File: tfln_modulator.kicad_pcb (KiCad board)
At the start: 12 copper layers, 300 x 140 mm, 981 parts

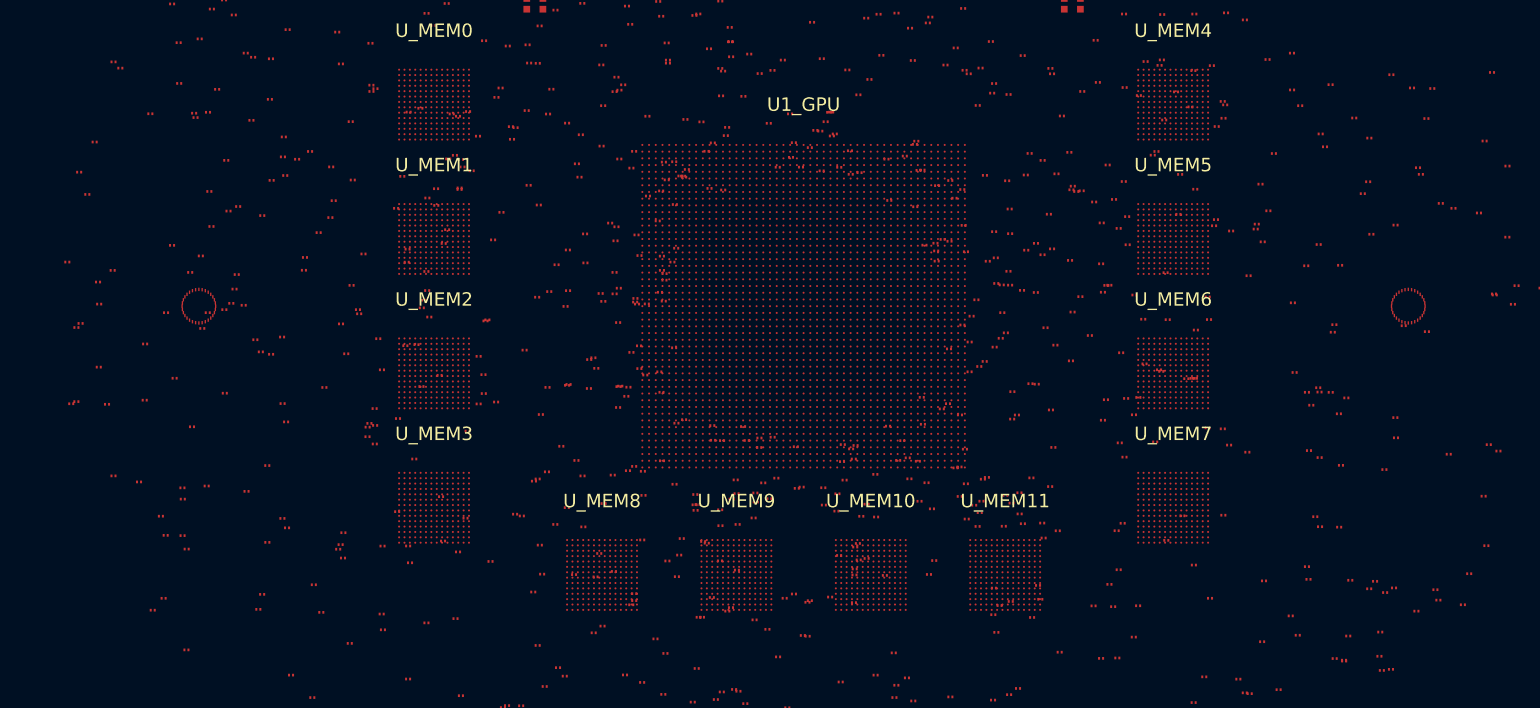
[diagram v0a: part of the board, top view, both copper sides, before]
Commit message: Generated 15-layer KiCad and Gerber files
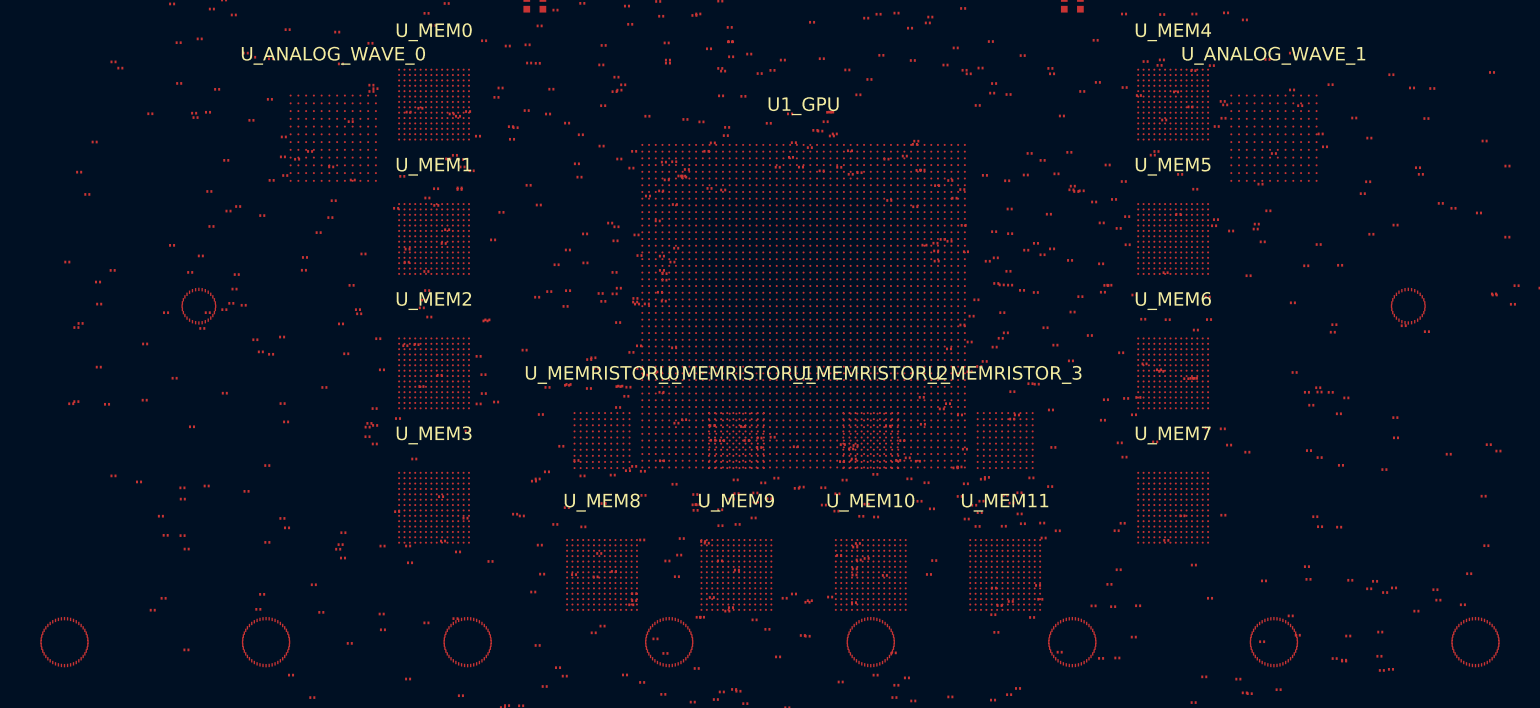
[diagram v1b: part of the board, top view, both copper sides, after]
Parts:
- added ?: , Package:QFN-48, F.Cu at (30.0, 120.0)
- added ?: , Package:QFN-48, F.Cu at (60.0, 120.0)
- added ?: , Package:QFN-48, F.Cu at (90.0, 120.0)
- added ?: , Package:QFN-48, F.Cu at (120.0, 120.0)
- added ?: , Package:QFN-48, F.Cu at (150.0, 120.0)
- added ?: , Package:QFN-48, F.Cu at (180.0, 120.0)
- added ?: , Package:QFN-48, F.Cu at (210.0, 120.0)
- added ?: , Package:QFN-48, F.Cu at (240.0, 120.0)
- added U_ANALOG_WAVE_0: , BGA:U_ANALOG_WAVE_0, F.Cu at (70.0, 45.0)
- added U_ANALOG_WAVE_1: , BGA:U_ANALOG_WAVE_1, F.Cu at (210.0, 45.0)
- added U_MEMRISTOR_0: , BGA:U_MEMRISTOR_0, F.Cu at (110.0, 90.0)
- added U_MEMRISTOR_1: , BGA:U_MEMRISTOR_1, F.Cu at (130.0, 90.0)
- added U_MEMRISTOR_2: , BGA:U_MEMRISTOR_2, F.Cu at (150.0, 90.0)
- added U_MEMRISTOR_3: , BGA:U_MEMRISTOR_3, F.Cu at (170.0, 90.0)
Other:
- copper layers 12 -> 15

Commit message: Increase component density to 2095 discrete components per user request
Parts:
- removed the ? at (177.6, 50.3)
- removed the ? at (178.6, 24.2)
- removed the ? at (206.0, 91.7)
- removed the ? at (235.9, 22.1)
- removed the ? at (154.4, 132.1)
- removed the ? at (192.3, 90.2)
- removed the ? at (193.9, 65.0)
- removed the ? at (149.3, 27.1)
- removed the ? at (86.0, 98.3)
- removed the ? at (246.1, 66.9)
- removed the ? at (130.2, 102.5)
- removed the ? at (45.8, 18.8)
- removed the ? at (118.3, 57.3)
- removed the ? at (179.3, 17.9)
- removed the ? at (173.1, 61.7)
- removed the ? at (150.7, 95.0)
- removed the ? at (170.0, 98.2)
- removed the ? at (86.2, 19.9)
- removed the ? at (90.1, 41.0)
- removed the ? at (201.5, 43.3)
- removed the ? at (131.9, 32.5)
- removed the ? at (107.1, 95.3)
- removed the ? at (140.6, 21.5)
- removed the ? at (114.4, 76.9)
- removed the ? at (249.8, 67.3)
- removed the ? at (146.1, 95.9)
- removed the ? at (180.1, 52.1)
- removed the ? at (169.2, 114.6)
- removed the ? at (214.8, 64.0)
- removed the ? at (218.8, 73.9)
- removed the ? at (213.9, 40.2)
- removed the ? at (164.0, 91.3)
- removed the ? at (112.0, 60.3)
- removed the ? at (104.8, 42.8)
- removed the ? at (193.0, 34.2)
- removed the ? at (220.4, 122.7)
- removed the ? at (130.3, 127.3)
- removed the ? at (142.7, 49.9)
- removed the ? at (57.8, 42.3)
- removed the ? at (198.4, 73.6)
- removed the ? at (159.9, 52.1)
- removed the ? at (42.8, 41.4)
- removed the ? at (57.4, 22.9)
- removed the ? at (163.2, 93.9)
- removed the ? at (178.4, 41.7)
- removed the ? at (173.9, 95.6)
- removed the ? at (207.3, 9.98)
- removed the ? at (98.9, 31.1)
- removed the ? at (170.7, 55.5)
- removed the ? at (236.7, 55.4)
- removed the ? at (208.3, 6.96)
- removed the ? at (138.1, 47.8)
- removed the ? at (185.3, 49.0)
- removed the ? at (210.7, 127.1)
- removed the ? at (156.3, 33.4)
- removed the ? at (119.1, 127.8)
- removed the ? at (147.7, 90.7)
- removed the ? at (172.6, 32.7)
- removed the ? at (77.2, 115.8)
- removed the ? at (34.5, 45.6)
- removed the ? at (112.7, 81.9)
- removed the ? at (65.6, 64.7)
- removed the ? at (91.5, 44.7)
- removed the ? at (129.0, 28.5)
- removed the ? at (158.0, 60.9)
- removed the ? at (187.8, 92.5)
- removed the ? at (167.9, 30.6)
- removed the ? at (99.9, 96.0)
- removed the ? at (124.1, 123.9)
- removed the ? at (112.4, 85.1)
- removed the ? at (95.0, 56.0)
- removed the ? at (135.4, 89.5)
- removed the ? at (88.6, 41.7)
- removed the ? at (63.0, 87.2)
- removed the ? at (153.5, 128.2)
- removed the ? at (190.9, 33.6)
- removed the ? at (112.5, 67.3)
- removed the ? at (177.5, 75.8)
- removed the ? at (98.5, 76.5)
- removed the ? at (226.6, 112.6)
- removed the ? at (100.7, 28.3)
- removed the ? at (127.6, 34.6)
- removed the ? at (142.4, 134.4)
- removed the ? at (219.0, 72.8)
- removed the ? at (113.6, 83.4)
- removed the ? at (174.6, 60.6)
- removed the ? at (203.3, 90.7)
- removed the ? at (164.6, 35.4)
- removed the ? at (159.4, 12.1)
- removed the ? at (219.8, 63.9)
- removed the ? at (210.0, 47.3)
- removed the ? at (55.3, 67.5)
- removed the ? at (49.5, 41.9)
- removed the ? at (136.4, 132.6)
- removed the ? at (112.6, 37.8)
- removed the ? at (51.9, 58.1)
- removed the ? at (134.0, 96.3)
- removed the ? at (121.1, 110.3)
- removed the ? at (184.3, 122.4)
- removed the ? at (125.9, 31.7)
- removed the ? at (216.9, 102.8)
- removed the ? at (85.3, 55.0)
- removed the ? at (155.4, 125.3)
- removed the ? at (187.8, 37.5)
- removed the ? at (194.2, 72.0)
- removed the ? at (141.1, 18.4)
- removed the ? at (232.7, 42.1)
- removed the ? at (139.1, 12.3)
- removed the ? at (84.9, 28.2)
- removed the ? at (147.6, 109.1)
- removed the ? at (216.6, 82.1)
- removed the ? at (198.2, 80.7)
- removed the ? at (118.4, 24.6)
- removed the ? at (168.7, 118.5)
- removed the ? at (183.2, 114.6)
- removed the ? at (214.9, 82.8)
- removed the ? at (89.0, 48.2)
- removed the ? at (126.0, 52.5)
- removed the ? at (108.7, 77.7)
- removed the ? at (122.2, 86.9)
- removed the ? at (121.9, 104.6)
- removed the ? at (147.5, 114.1)
- removed the ? at (75.8, 130.9)
- removed the ? at (177.2, 91.0)
- removed the ? at (118.9, 64.7)
- removed the ? at (152.6, 87.9)
- removed the ? at (124.8, 42.6)
- removed the ? at (112.6, 48.1)
- removed the ? at (205.7, 127.5)
- removed the ? at (231.4, 49.4)
- removed the ? at (169.3, 74.8)
- removed the ? at (118.8, 26.8)
- removed the ? at (225.7, 122.1)
- removed the ? at (55.4, 134.2)
- removed the ? at (214.9, 108.8)
- removed the ? at (82.7, 11.1)
- removed the ? at (144.1, 41.1)
- removed the ? at (62.1, 13.1)
- removed the ? at (170.7, 66.9)
- removed the ? at (99.8, 112.5)
- removed the ? at (104.5, 125.1)
- removed the ? at (168.6, 62.8)
- removed the ? at (63.1, 103.0)
- removed the ? at (197.0, 80.8)
- removed the ? at (224.0, 51.5)
- removed the ? at (155.8, 28.6)
- removed the ? at (71.9, 77.1)
- removed the ? at (133.0, 11.2)
- removed the ? at (166.3, 34.6)
- removed the ? at (221.1, 119.1)
- removed the ? at (92.4, 30.5)
- removed the ? at (193.2, 79.7)
- removed the ? at (151.6, 32.7)
- removed the ? at (177.0, 35.4)
- removed the ? at (100.3, 68.7)
- removed the ? at (159.8, 63.3)
- removed the ? at (134.8, 42.8)
- removed the ? at (143.3, 6.11)
- removed the ? at (157.1, 8.15)
- removed the ? at (145.0, 97.9)
- removed the ? at (68.7, 82.1)
- removed the ? at (79.5, 100.6)
- removed the ? at (171.0, 99.3)
- removed the ? at (167.3, 95.5)
- removed the ? at (147.7, 105.8)
- removed the ? at (147.1, 91.2)
- removed the ? at (129.9, 7.23)
- removed the ? at (33.4, 53.4)
- removed the ? at (176.7, 96.8)
- removed the ? at (145.3, 107.1)
- removed the ? at (176.0, 73.2)
- removed the ? at (38.3, 34.6)
- removed the ? at (198.1, 129.0)
- removed the ? at (42.0, 75.6)
- removed the ? at (51.9, 25.8)
- removed the ? at (82.1, 92.7)
- removed the ? at (64.6, 48.1)
- removed the ? at (174.7, 81.6)
- removed the ? at (36.3, 84.6)
- removed the ? at (63.7, 124.9)
- removed the ? at (121.7, 50.6)
- removed the ? at (154.7, 90.0)
- removed the ? at (70.3, 15.0)
- removed the ? at (76.2, 90.5)
- removed the ? at (178.2, 23.9)
- removed the ? at (81.4, 21.8)
- removed the ? at (222.0, 42.0)
- removed the ? at (106.3, 48.8)
- removed the ? at (149.4, 107.5)
- removed the ? at (171.8, 86.2)
- removed the ? at (120.7, 76.2)
- removed the ? at (129.1, 30.7)
- removed the ? at (60.2, 93.7)
- removed the ? at (212.7, 32.3)
- removed the ? at (75.7, 5.70)
- removed the ? at (212.7, 37.8)
- removed the ? at (84.0, 53.9)
- removed the ? at (205.7, 27.4)
- removed the ? at (232.8, 73.8)
- removed the ? at (225.1, 110.9)
- removed the ? at (127.6, 102.7)
- removed the ? at (60.7, 33.2)
- removed the ? at (172.6, 102.4)
- removed the ? at (35.2, 69.7)
- removed the ? at (196.4, 101.2)
- removed the ? at (118.5, 79.8)
- removed the ? at (139.9, 119.0)
- removed the ? at (167.4, 63.3)
- removed the ? at (55.2, 26.7)
- removed the ? at (168.3, 112.0)
- removed the ? at (245.6, 69.7)
- removed the ? at (140.9, 46.4)
- removed the ? at (103.8, 19.2)
- removed the ? at (91.9, 15.5)
- removed the ? at (194.0, 104.9)
- removed the ? at (114.3, 114.4)
- removed the ? at (190.3, 7.40)
- removed the ? at (122.8, 23.4)
- removed the ? at (183.2, 54.5)
- removed the ? at (51.4, 41.1)
- removed the ? at (163.3, 86.2)
- removed the ? at (116.0, 126.0)
- removed the ? at (188.2, 60.9)
- removed the ? at (83.9, 64.8)
- removed the ? at (81.1, 105.7)
- removed the ? at (116.2, 98.2)
- removed the ? at (77.9, 7.56)
- removed the ? at (202.4, 39.5)
- removed the ? at (121.0, 13.7)
- removed the ? at (170.5, 64.8)
- removed the ? at (107.5, 59.2)
- removed the ? at (63.5, 11.6)
- removed the ? at (198.1, 108.5)
- removed the ? at (233.3, 13.1)
- removed the ? at (185.5, 111.4)
- removed the ? at (45.1, 71.0)
- removed the ? at (55.6, 65.3)
- removed the ? at (162.6, 31.6)
- removed the ? at (88.2, 116.5)
- removed the ? at (37.2, 64.7)
- removed the ? at (151.2, 26.5)
- removed the ? at (192.5, 47.0)
- removed the ? at (207.3, 58.5)
- removed the ? at (168.2, 10.7)
- removed the ? at (126.3, 113.4)
- removed the ? at (212.8, 69.5)
- removed the ? at (178.1, 121.5)
- removed the ? at (101.5, 126.6)
- removed the ? at (72.9, 51.2)
- removed the ? at (113.4, 124.9)
- removed the ? at (128.0, 35.0)
- removed the ? at (226.4, 94.3)
- removed the ? at (69.8, 131.0)
- removed the ? at (88.8, 52.6)
- removed the ? at (31.8, 73.2)
- removed the ? at (116.7, 69.7)
- removed the ? at (190.0, 16.6)
- removed the ? at (48.2, 106.1)
- removed the ? at (75.1, 88.0)
- removed the ? at (68.2, 115.6)
- removed the ? at (201.1, 58.0)
- removed the ? at (122.2, 22.8)
- removed the ? at (186.8, 7.02)
- removed the ? at (118.0, 119.5)
- removed the ? at (70.4, 5.86)
- removed the ? at (236.0, 92.0)
- removed the ? at (122.2, 50.8)
- removed the ? at (242.9, 68.3)
- removed the ? at (60.2, 105.2)
- removed the ? at (120.7, 48.5)
- removed the ? at (47.6, 104.1)
- removed the ? at (207.7, 23.0)
- removed the ? at (146.9, 46.9)
- removed the ? at (107.2, 102.8)
- removed the ? at (107.5, 63.6)
- removed the ? at (53.7, 24.4)
- removed the ? at (171.0, 86.8)
- removed the ? at (175.6, 48.3)
- removed the ? at (108.1, 77.9)
- removed the ? at (138.6, 112.8)
- removed the ? at (147.0, 50.4)
- removed the ? at (108.0, 82.2)
- removed the ? at (96.4, 43.3)
- removed the ? at (71.1, 105.5)
- removed the ? at (164.0, 34.9)
- removed the ? at (111.6, 95.1)
- removed the ? at (220.0, 93.7)
- removed the ? at (145.1, 133.3)
- removed the ? at (76.3, 37.6)
- removed the ? at (99.1, 52.0)
- removed the ? at (120.8, 54.9)
- removed the ? at (193.3, 33.3)
- removed the ? at (153.8, 26.4)
- removed the ? at (95.3, 129.7)
- removed the ? at (84.0, 16.8)
- removed the ? at (202.9, 26.3)
- removed the ? at (87.6, 41.4)
- removed the ? at (130.1, 109.3)
- removed the ? at (212.5, 116.1)
- removed the ? at (139.3, 23.4)
- removed the ? at (164.2, 96.4)
- removed the ? at (207.4, 57.8)
- removed the ? at (198.0, 34.9)
- removed the ? at (46.4, 80.7)
- removed the ? at (177.8, 103.4)
- removed the ? at (224.5, 59.3)
- removed the ? at (153.4, 18.8)
- removed the ? at (119.3, 65.2)
- removed the ? at (142.9, 97.0)
- removed the ? at (111.6, 16.1)
- removed the ? at (70.6, 29.2)
- removed the ? at (227.5, 35.5)
- removed the ? at (143.0, 99.6)
- removed the ? at (156.6, 55.2)
- removed the ? at (200.8, 34.2)
- removed the ? at (176.8, 85.4)
- removed the ? at (219.3, 19.2)
- removed the ? at (100.4, 95.7)
- removed the ? at (170.7, 59.2)
- removed the ? at (134.9, 98.6)
- removed the ? at (92.7, 72.2)
- removed the ? at (161.8, 51.3)
- removed the ? at (109.1, 79.2)
- removed the ? at (48.1, 121.2)
- removed the ? at (186.6, 103.4)
- removed the ? at (86.3, 105.0)
- removed the ? at (243.4, 91.6)
- removed the ? at (90.0, 88.6)
- removed the ? at (128.6, 43.4)
- removed the ? at (208.3, 60.4)
- removed the ? at (89.0, 128.0)
- removed the ? at (98.1, 101.2)
- removed the ? at (166.7, 95.7)
- removed the ? at (47.5, 97.0)
- removed the ? at (89.9, 8.09)
- removed the ? at (213.1, 79.9)
- removed the ? at (111.2, 57.6)
- removed the ? at (142.5, 43.9)
- removed the ? at (148.2, 107.8)
- removed the ? at (167.0, 50.5)
- removed the ? at (152.8, 54.3)
- removed the ? at (153.4, 121.6)
- removed the ? at (162.6, 94.1)
- removed the ? at (159.4, 107.9)
- removed the ? at (218.5, 82.8)
- removed the ? at (145.3, 49.3)
- removed the ? at (121.5, 107.0)
- removed the ? at (173.8, 81.5)
- removed the ? at (54.4, 55.8)
- removed the ? at (53.9, 83.0)
- removed the ? at (50.3, 62.5)
- removed the ? at (110.2, 69.3)
- removed the ? at (180.6, 52.9)
- removed the ? at (241.2, 98.3)
- removed the ? at (75.4, 87.4)
- removed the ? at (239.1, 109.8)
- removed the ? at (88.6, 106.6)
- removed the ? at (58.4, 75.0)
- removed the ? at (231.2, 115.4)
- removed the ? at (118.8, 52.8)
- removed the ? at (135.9, 95.6)
- removed the ? at (66.5, 47.0)
- removed the ? at (189.2, 68.3)
- removed the ? at (79.4, 20.4)
- removed the ? at (75.1, 89.4)
- removed the ? at (200.5, 113.5)
- removed the ? at (148.2, 130.1)
- removed the ? at (91.6, 84.5)
- removed the ? at (187.5, 102.3)
- removed the ? at (110.3, 19.7)
- removed the ? at (170.8, 114.0)
- removed the ? at (234.0, 112.2)
- removed the ? at (219.0, 122.4)
- removed the ? at (138.0, 41.4)
- removed the ? at (135.4, 34.9)
- removed the ? at (52.7, 37.7)
- removed the ? at (72.6, 42.5)
- removed the ? at (175.7, 104.5)
- removed the ? at (113.7, 25.3)
- removed the ? at (199.1, 5.48)
- removed the ? at (223.2, 53.3)
- removed the ? at (95.9, 129.4)
- removed the ? at (156.8, 45.4)
- removed the ? at (144.2, 17.1)
- removed the ? at (234.8, 54.7)
- removed the ? at (114.8, 93.8)
- removed the ? at (69.2, 8.70)
- removed the ? at (216.8, 82.8)
- removed the ? at (158.7, 109.9)
- removed the ? at (190.5, 71.9)
- removed the ? at (50.1, 30.2)
- removed the ? at (175.2, 113.6)
- removed the ? at (215.6, 84.7)
- removed the ? at (108.8, 118.6)
- removed the ? at (130.5, 17.5)
- removed the ? at (58.1, 33.0)
- removed the ? at (112.0, 5.71)
- removed the ? at (166.1, 79.0)
- removed the ? at (114.8, 47.0)
- removed the ? at (60.7, 77.2)
- removed the ? at (131.3, 129.2)
- removed the ? at (206.4, 127.7)
- removed the ? at (127.8, 127.4)
- removed the ? at (59.2, 76.8)
- removed the ? at (216.8, 92.5)
- removed the ? at (94.9, 37.5)
- removed the ? at (133.4, 89.6)
- removed the ? at (179.8, 78.1)
- removed the ? at (165.4, 99.6)
- removed the ? at (119.7, 107.9)
- removed the ? at (139.6, 49.3)
- removed the ? at (113.9, 94.5)
- removed the ? at (56.7, 69.9)
- removed the ? at (157.1, 49.8)
- removed the ? at (163.6, 72.8)
- removed the ? at (75.7, 38.0)
- removed the ? at (67.1, 111.5)
- removed the ? at (170.1, 74.0)
- removed the ? at (134.6, 118.1)
- removed the ? at (155.6, 23.3)
- removed the ? at (227.4, 124.0)
- removed the ? at (67.8, 59.1)
- removed the ? at (119.4, 121.7)
- removed the ? at (114.8, 113.8)
- removed the ? at (104.9, 67.7)
- removed the ? at (109.8, 68.1)
- removed the ? at (150.8, 101.4)
- removed the ? at (50.5, 73.3)
- removed the ? at (193.7, 42.3)
- removed the ? at (176.5, 56.3)
- removed the ? at (93.3, 16.8)
- removed the ? at (190.1, 12.6)
- removed the ? at (184.6, 132.1)
- removed the ? at (115.6, 79.3)
- removed the ? at (132.7, 116.7)
- removed the ? at (115.0, 68.8)
- removed the ? at (94.2, 84.3)
- removed the ? at (152.3, 48.1)
- removed the ? at (157.7, 49.7)
- removed the ? at (67.3, 5.87)
- removed the ? at (77.4, 118.2)
- removed the ? at (76.2, 85.2)
- removed the ? at (44.3, 101.3)
- removed the ? at (91.6, 77.5)
- removed the ? at (171.1, 82.7)
- removed the ? at (163.6, 52.6)
- removed the ? at (128.7, 20.4)
- removed the ? at (170.6, 127.8)
- removed the ? at (100.9, 86.1)
- removed the ? at (81.1, 61.5)
- removed the ? at (116.1, 94.6)
- removed the ? at (41.1, 96.2)
- removed the ? at (101.8, 94.7)
- removed the ? at (98.8, 40.9)
- removed the ? at (161.5, 84.5)
- removed the ? at (96.6, 45.2)
- removed the ? at (120.8, 96.5)
- removed the ? at (94.3, 38.9)
- removed the ? at (153.9, 17.9)
- removed the ? at (59.4, 56.5)
- removed the ? at (70.7, 106.2)
- removed the ? at (105.8, 109.9)
- removed the ? at (140.9, 113.8)
- removed the ? at (148.1, 105.3)
- removed the ? at (35.1, 79.1)
- removed the ? at (166.2, 100.7)
- removed the ? at (155.1, 47.7)
- removed the ? at (143.8, 41.1)
- removed the ? at (210.9, 6.48)
- removed the ? at (127.9, 90.0)
- removed the ? at (168.2, 115.9)
- removed the ? at (89.7, 101.6)
- removed the ? at (126.9, 128.5)
- removed the ? at (198.2, 26.5)
- removed the ? at (57.1, 97.6)
- removed the ? at (115.2, 133.4)
- removed the ? at (49.0, 87.9)
- removed the ? at (244.7, 59.7)
- removed the ? at (127.8, 130.3)
- removed the ? at (86.4, 60.7)
- removed the ? at (113.2, 37.1)
- removed the ? at (47.1, 36.8)
- removed the ? at (156.6, 45.9)
- removed the ? at (196.0, 50.4)
- removed the ? at (150.7, 124.9)
- removed the ? at (101.9, 82.1)
- removed the ? at (190.7, 78.6)
- removed the ? at (115.2, 69.7)
- removed the ? at (181.2, 68.6)
- removed the ? at (192.9, 79.5)
- removed the ? at (132.6, 101.5)
- removed the ? at (131.0, 38.8)
- removed the ? at (200.3, 72.0)
- removed the ? at (139.0, 97.1)
- removed the ? at (49.3, 41.3)
- removed the ? at (30.4, 63.4)
- removed the ? at (55.8, 55.2)
- removed the ? at (132.9, 99.2)
- removed the ? at (185.0, 83.9)
- removed the ? at (155.7, 14.4)
- removed the ? at (186.9, 109.2)
- removed the ? at (56.7, 12.1)
- removed the ? at (118.6, 67.9)
- removed the ? at (165.9, 102.8)
- removed the ? at (96.0, 31.3)
- removed the ? at (103.9, 90.8)
- removed the ? at (167.0, 78.2)
- removed the ? at (208.5, 110.9)
- removed the ? at (238.1, 114.4)
- removed the ? at (72.7, 66.9)
- removed the ? at (37.3, 33.6)
- removed the ? at (85.8, 80.3)
- removed the ? at (216.7, 60.8)
- removed the ? at (182.6, 74.4)
- removed the ? at (80.5, 7.98)
- removed the ? at (188.0, 83.7)
- removed the ? at (166.9, 6.29)
- removed the ? at (119.2, 48.6)
- removed the ? at (146.5, 34.8)
- removed the ? at (119.2, 11.8)
- removed the ? at (144.2, 44.7)
- removed the ? at (123.5, 128.9)
- removed the ? at (147.5, 92.7)
- removed the ? at (161.7, 60.3)
- removed the ? at (206.2, 65.5)
- removed the ? at (150.0, 18.8)
- removed the ? at (118.9, 93.0)
- removed the ? at (32.4, 72.6)
- removed the ? at (59.4, 112.9)
- removed the ? at (197.6, 40.3)
- removed the ? at (161.1, 6.68)
- removed the ? at (215.1, 110.7)
- removed the ? at (110.1, 132.3)
- removed the ? at (125.6, 46.9)
- removed the ? at (102.0, 41.4)
- removed the ? at (118.4, 15.8)
- removed the ? at (189.8, 83.6)
- removed the ? at (242.5, 35.2)
- removed the ? at (122.6, 49.7)
- removed the ? at (121.1, 87.4)
- removed the ? at (156.6, 20.0)
- removed the ? at (217.6, 46.3)
- removed the ? at (114.4, 49.4)
- removed the ? at (228.2, 89.6)
- removed the ? at (144.6, 44.4)
- removed the ? at (100.7, 105.6)
- removed the ? at (83.9, 26.4)
- removed the ? at (217.0, 44.4)
- removed the ? at (144.4, 16.7)
- removed the ? at (69.6, 56.8)
- removed the ? at (32.2, 50.1)
- removed the ? at (107.1, 24.9)
- removed the ? at (172.1, 97.8)
- removed the ? at (53.8, 70.5)
- removed the ? at (89.2, 49.3)
- removed the ? at (137.2, 113.5)
- removed the ? at (200.1, 68.6)
- removed the ? at (179.6, 47.1)
- removed the ? at (186.1, 114.7)
- removed the ? at (47.6, 98.7)
- removed the ? at (45.1, 104.1)
- removed the ? at (136.2, 49.3)
- removed the ? at (128.4, 44.6)
- removed the ? at (187.1, 90.3)
- removed the ? at (193.4, 26.6)
- removed the ? at (48.7, 65.0)
- removed the ? at (149.4, 99.5)
- removed the ? at (148.2, 38.5)
- removed the ? at (118.9, 62.6)
- removed the ? at (157.6, 19.8)
- removed the ? at (86.9, 25.0)
- removed the ? at (129.9, 95.9)
- removed the ? at (60.8, 51.3)
- removed the ? at (224.2, 112.1)
- removed the ? at (114.3, 15.2)
- removed the ? at (176.7, 34.6)
- removed the ? at (175.6, 62.3)
- removed the ? at (189.9, 38.6)
- removed the ? at (157.8, 87.6)
- removed the ? at (157.3, 99.0)
- removed the ? at (127.6, 22.6)
- removed the ? at (187.7, 51.4)
- removed the ? at (111.9, 38.1)
- removed the ? at (112.2, 35.9)
- removed the ? at (189.1, 119.2)
- removed the ? at (93.8, 60.1)
- removed the ? at (171.9, 126.9)
- removed the ? at (180.9, 7.77)
- removed the ? at (172.2, 7.03)
- removed the ? at (161.6, 76.4)
- removed the ? at (71.1, 33.9)
- removed the ? at (103.1, 25.9)
- removed the ? at (94.8, 23.5)
- removed the ? at (184.4, 57.6)
- removed the ? at (112.4, 82.0)
- removed the ? at (161.4, 10.2)
- removed the ? at (164.7, 79.8)
- removed the ? at (80.7, 75.9)
- removed the ? at (109.9, 46.2)
- removed the ? at (130.5, 22.8)
- removed the ? at (90.6, 49.8)
- removed the ? at (92.4, 80.2)
- removed the ? at (140.6, 114.1)
- removed the ? at (132.8, 97.8)
- removed the ? at (99.2, 33.8)
- removed the ? at (198.3, 52.6)
- removed the ? at (168.1, 38.3)
- removed the ? at (123.9, 100.4)
- removed the ? at (51.3, 71.0)
- removed the ? at (73.7, 70.5)
- removed the ? at (187.3, 76.9)
- removed the ? at (35.0, 66.4)
- removed the ? at (189.2, 86.2)
- removed the ? at (187.7, 26.5)
- removed the ? at (62.5, 84.5)
- removed the ? at (179.2, 14.0)
- removed the ? at (168.2, 128.6)
- removed the ? at (183.5, 30.4)
- removed the ? at (97.1, 101.0)
- removed the ? at (202.5, 101.1)
- removed the ? at (185.1, 66.9)
- removed the ? at (199.6, 125.2)
- removed the ? at (102.1, 67.8)
- removed the ? at (202.4, 88.3)
- removed the ? at (123.9, 98.0)
- removed the ? at (79.6, 86.7)
- removed the ? at (65.8, 62.7)
- removed the ? at (109.9, 34.1)
- removed the ? at (102.5, 37.7)
- removed the ? at (174.6, 68.0)
- removed the ? at (163.7, 25.7)
- removed the ? at (158.9, 27.0)
- removed the ? at (115.5, 22.8)
- removed the ? at (46.4, 15.7)
- removed the ? at (220.8, 83.7)
- removed the ? at (201.4, 57.1)
- removed the ? at (174.7, 133.7)
- removed the ? at (84.1, 17.6)
- removed the ? at (182.9, 131.3)
- removed the ? at (219.7, 86.0)
- removed the ? at (131.5, 90.0)
- removed the ? at (127.7, 38.7)
- removed the ? at (148.9, 13.8)
- removed the ? at (219.7, 102.9)
- removed the ? at (148.6, 101.3)
- removed the ? at (114.2, 28.0)
- removed the ? at (113.8, 132.0)
- removed the ? at (170.3, 51.3)
- removed the ? at (109.0, 110.3)
- removed the ? at (54.1, 48.3)
- removed the ? at (100.6, 54.9)
- removed the ? at (179.7, 63.2)
- removed the ? at (128.6, 115.4)
- removed the ? at (129.2, 32.9)
- removed the ? at (111.8, 109.5)
- removed the ? at (172.2, 100.9)
- removed the ? at (81.1, 125.5)
- removed the ? at (129.2, 114.9)
- removed the ? at (137.6, 129.8)
- removed the ? at (158.7, 130.3)
- removed the ? at (51.6, 52.9)
- removed the ? at (202.5, 42.0)
- removed the ? at (193.8, 132.8)
- removed the ? at (75.5, 30.9)
- removed the ? at (119.8, 33.4)
- removed the ? at (96.1, 18.3)
- removed the ? at (118.9, 82.8)
- removed the ? at (208.2, 119.9)
- removed the ? at (229.3, 72.9)
- removed the ? at (202.7, 40.0)
- removed the ? at (192.0, 47.5)
- removed the ? at (131.0, 87.9)
- removed the ? at (41.9, 84.0)
- removed the ? at (177.0, 61.5)
- removed the ? at (110.2, 31.2)
- removed the ? at (226.1, 124.2)
- removed the ? at (70.1, 54.3)
- removed the ? at (218.4, 37.0)
- removed the ? at (242.8, 68.2)
- removed the ? at (84.3, 71.6)
- removed the ? at (241.4, 45.4)
- removed the ? at (121.0, 61.4)
- removed the ? at (159.6, 60.6)
- removed the ? at (169.5, 66.8)
- removed the ? at (185.5, 66.9)
- removed the ? at (71.2, 72.6)
- removed the ? at (161.8, 128.2)
- removed the ? at (155.7, 95.7)
- removed the ? at (137.2, 131.2)
- removed the ? at (136.9, 33.4)
- removed the ? at (57.0, 32.3)
- removed the ? at (217.4, 11.5)
- removed the ? at (46.0, 60.9)
- removed the ? at (184.6, 87.0)
- removed the ? at (126.5, 45.7)
- removed the ? at (163.2, 98.3)
- removed the ? at (140.6, 119.1)
- removed the ? at (143.9, 113.3)
- removed the ? at (224.2, 45.0)
- removed the ? at (132.0, 23.5)
- removed the ? at (128.0, 52.7)
- removed the ? at (216.2, 101.3)
- removed the ? at (129.3, 98.7)
- removed the ? at (83.5, 69.1)
- removed the ? at (233.6, 37.6)
- removed the ? at (175.5, 102.3)
- removed the ? at (158.3, 96.3)
- removed the ? at (71.3, 16.2)
- removed the ? at (85.3, 52.5)
- removed the ? at (79.4, 55.4)
- removed the ? at (141.3, 27.7)
- removed the ? at (225.8, 118.5)
- removed the ? at (122.8, 12.3)
- removed the ? at (115.1, 59.4)
- removed the ? at (115.6, 62.5)
- removed the ? at (112.4, 72.4)
- removed the ? at (81.2, 41.1)
- removed the ? at (124.2, 99.5)
- removed the ? at (189.8, 114.6)
- removed the ? at (106.6, 50.8)
- removed the ? at (111.9, 68.2)
- removed the ? at (51.2, 96.8)
- removed the ? at (76.2, 87.7)
- removed the ? at (115.5, 75.9)
- removed the ? at (162.6, 19.1)
- removed the ? at (63.2, 28.8)
- removed the ? at (141.7, 43.8)
- removed the ? at (126.5, 90.0)
- removed the ? at (165.7, 69.0)
- removed the ? at (234.5, 113.7)
- removed the ? at (242.0, 90.6)
- removed the ? at (146.8, 13.6)
- removed the ? at (228.1, 57.9)
- removed the ? at (71.4, 107.5)
- removed the ? at (221.9, 15.7)
- removed the ? at (117.9, 20.9)
- removed the ? at (62.9, 50.6)
- removed the ? at (201.5, 134.2)
- removed the ? at (94.6, 134.4)
- removed the ? at (104.9, 61.6)
- removed the ? at (180.0, 70.9)
- removed the ? at (133.4, 91.0)
- removed the ? at (62.5, 47.8)
- removed the ? at (170.2, 9.21)
- removed the ? at (116.0, 104.8)
- removed the ? at (181.4, 52.8)
- removed the ? at (204.7, 125.5)
- removed the ? at (58.8, 115.1)
- removed the ? at (80.3, 50.7)
- removed the ? at (206.3, 10.7)
- removed the ? at (145.8, 90.6)
- removed the ? at (168.4, 76.1)
- removed the ? at (138.6, 45.7)
- removed the ? at (145.5, 125.9)
- removed the ? at (165.9, 40.1)
- removed the ? at (114.9, 69.4)
- removed the ? at (158.5, 27.8)
- removed the ? at (124.4, 116.3)
- removed the ? at (122.4, 42.2)
- removed the ? at (170.5, 38.5)
- removed the ? at (127.6, 107.9)
- removed the ? at (164.2, 61.9)
- removed the ? at (224.3, 17.7)
- removed the ? at (71.5, 103.7)
- removed the ? at (203.6, 58.8)
- removed the ? at (174.0, 116.3)
- removed the ? at (141.5, 16.1)
- removed the ? at (176.6, 19.2)
- removed the ? at (127.6, 24.6)
- removed the ? at (219.6, 22.8)
- removed the ? at (153.8, 126.4)
- removed the ? at (209.2, 55.8)
- removed the ? at (186.7, 122.4)
- removed the ? at (152.1, 110.1)
- removed the ? at (209.1, 33.3)
- removed the ? at (220.5, 122.8)
- removed the ? at (119.6, 30.8)
- removed the ? at (192.1, 17.0)
- removed the ? at (142.7, 33.2)
- removed the ? at (60.6, 39.2)
- removed the ? at (183.1, 23.8)
- removed the ? at (125.6, 105.3)
- removed the ? at (188.2, 56.7)
- removed the ? at (159.7, 61.8)
- removed the ? at (31.0, 84.5)
- removed the ? at (106.8, 44.5)
- removed the ? at (173.1, 50.5)
- removed the ? at (86.9, 58.6)
- removed the ? at (136.2, 122.2)
- removed the ? at (73.9, 71.1)
- removed the ? at (168.7, 66.6)
- removed the ? at (173.3, 17.4)
- removed the ? at (80.9, 63.5)
- removed the ? at (87.1, 48.1)
- removed the ? at (164.3, 101.7)
- removed the ? at (179.9, 52.7)
- removed the ? at (77.3, 105.7)
- removed the ? at (123.8, 99.6)
- removed the ? at (167.1, 23.1)
- removed the ? at (103.4, 16.4)
- removed the ? at (231.9, 50.4)
- removed the ? at (62.4, 74.6)
- removed the ? at (149.8, 36.3)
- removed the ? at (144.9, 100.5)
- removed the ? at (133.5, 35.4)
- removed the ? at (195.4, 38.1)
- removed the ? at (96.8, 16.5)
- removed the ? at (164.7, 75.3)
- removed the ? at (230.6, 37.5)
- removed the ? at (171.4, 22.3)
- removed the ? at (129.1, 30.6)
- removed the ? at (119.2, 69.2)
- removed the ? at (100.4, 33.9)
- removed the ? at (80.5, 16.5)
- removed the ? at (97.1, 43.4)
- removed the ? at (76.7, 74.8)
- removed the ? at (120.5, 63.4)
- removed the ? at (119.3, 66.1)
- removed the ? at (184.3, 63.7)
- removed the ? at (148.3, 50.1)
- removed the ? at (219.7, 133.5)
- removed the ? at (157.0, 93.1)
- removed the ? at (103.2, 63.8)
- removed the ? at (101.1, 109.9)
- removed the ? at (88.1, 47.5)
- removed the ? at (147.6, 110.0)
- removed the ? at (189.6, 8.70)
- removed the ? at (213.5, 119.0)
- removed the ? at (88.8, 52.4)
- removed the ? at (165.0, 71.5)
- removed the ? at (104.6, 70.0)
- removed the ? at (152.7, 12.3)
- removed the ? at (184.5, 14.8)
- removed the ? at (111.9, 65.0)
- removed the ? at (145.7, 93.1)
- removed the ? at (214.6, 6.29)
- removed the ? at (122.1, 50.6)
- removed the ? at (200.1, 88.1)
- removed the ? at (163.8, 58.0)
- removed the ? at (47.0, 30.8)
- removed the ? at (160.7, 60.1)
- removed the ? at (186.9, 58.4)
- removed the ? at (72.5, 120.2)
- removed the ? at (154.1, 93.0)
- removed the ? at (161.1, 34.1)
- removed the ? at (183.8, 36.7)
- removed the ? at (141.8, 20.2)
- removed the ? at (173.6, 47.3)
- removed the ? at (172.5, 67.6)
- removed the ? at (54.8, 69.6)
- removed the ? at (241.6, 105.6)
- removed the ? at (171.4, 19.6)
- removed the ? at (146.0, 19.7)
- removed the ? at (55.6, 134.0)
- removed the ? at (228.1, 86.6)
- removed the ? at (184.6, 67.9)
- removed the ? at (100.4, 120.5)
- removed the ? at (44.8, 113.5)
- removed the ? at (227.9, 111.9)
- removed the ? at (119.6, 51.2)
- removed the ? at (155.5, 92.6)
- removed the ? at (84.0, 7.34)
- removed the ? at (169.6, 71.0)
- removed the ? at (109.6, 106.8)
- removed the ? at (169.8, 102.8)
- removed the ? at (105.0, 81.6)
- removed the ? at (81.4, 108.2)
- removed the ? at (126.4, 87.8)
- removed the ? at (116.8, 53.6)
- removed the ? at (119.8, 33.8)
- removed the ? at (103.0, 102.5)
- removed the ? at (104.8, 100.0)
- removed the ? at (162.5, 53.9)
- removed the ? at (240.5, 56.1)
- removed the ? at (174.6, 132.5)
- removed the ? at (174.9, 111.6)
- removed the ? at (92.9, 72.0)
- removed the ? at (116.4, 80.3)
- removed the ? at (82.4, 75.7)
- removed the ? at (139.7, 96.9)
- removed the ? at (166.5, 99.0)
- removed the ? at (110.2, 40.2)
- removed the ? at (130.0, 97.9)
- removed the ? at (114.8, 112.8)
- removed the ? at (186.2, 54.1)
- removed the ? at (125.1, 105.0)
- removed the ? at (244.8, 49.1)
- removed the ? at (124.3, 26.5)
- removed the ? at (83.0, 40.5)
- removed the ? at (110.2, 99.4)
- removed the ? at (66.9, 128.3)
- removed the ? at (46.0, 25.0)
- removed the ? at (112.2, 58.2)
- removed the ? at (69.7, 49.3)
- removed the ? at (62.6, 44.8)
- removed the ? at (37.3, 95.3)
- removed the ? at (62.4, 101.6)
- removed the ? at (123.8, 26.7)
- removed the ? at (83.2, 70.2)
- removed the ? at (221.4, 110.8)
- removed the ? at (31.8, 84.2)
- removed the ? at (84.0, 67.7)
- removed the ? at (153.5, 8.93)
- removed the ? at (181.5, 38.0)
- removed the ? at (95.9, 17.9)
- removed the ? at (143.3, 42.5)
- removed the ? at (91.5, 132.6)
- removed the ? at (215.2, 91.5)
- removed the ? at (140.9, 14.0)
- removed the ? at (43.1, 115.2)
- removed the ? at (138.8, 90.9)
- removed the ? at (74.5, 62.2)
- removed the ? at (75.7, 37.1)
- removed the ? at (113.9, 82.1)
- removed the ? at (93.4, 108.0)
- removed the ? at (64.0, 22.7)
- removed the ? at (103.5, 123.8)
- removed the ? at (157.6, 83.6)
- removed the ? at (195.8, 56.3)
- removed the ? at (168.4, 58.9)
- removed the ? at (127.6, 100.3)
- removed the ? at (156.3, 128.8)
- removed the ? at (77.2, 79.5)
- removed the ? at (120.5, 13.9)
- removed the ? at (83.1, 82.0)
- removed the ? at (124.9, 116.3)
- removed the ? at (209.7, 131.5)
- removed the ? at (159.1, 100.2)
- removed the ? at (208.0, 51.8)
- removed the ? at (106.2, 93.0)
- removed the ? at (116.8, 41.7)
- removed the ? at (197.9, 80.7)
- removed the ? at (83.9, 117.1)
- removed the ? at (160.6, 85.3)
- removed the ? at (92.4, 83.0)
- removed the ? at (228.5, 132.9)
- removed the ? at (168.4, 36.9)
- removed the ? at (96.7, 18.2)
- removed the ? at (83.6, 22.5)
- removed the ? at (98.0, 129.5)
- removed the ? at (68.9, 5.39)
- removed the ? at (110.1, 117.6)
- removed the ? at (104.8, 81.8)
- removed the ? at (129.7, 127.0)
- added ?: , SMD:0402, F.Cu at (217.0, 136.7)
- added ?: , SMD:0402, F.Cu at (137.7, 107.6)
- added ?: , SMD:0402, F.Cu at (219.2, 24.6)
- added ?: , SMD:0201, F.Cu at (58.0, 22.2)
- added ?: , SMD:0201, F.Cu at (36.6, 119.7)
- added ?: , SMD:0201, F.Cu at (235.2, 100.1)
- added ?: , SMD:0201, F.Cu at (195.9, 132.9)
- added ?: , SMD:0402, F.Cu at (148.6, 58.3)
- added ?: , SMD:0201, F.Cu at (55.1, 21.4)
- added ?: , SMD:0201, F.Cu at (164.3, 8.33)
- added ?: , SMD:0201, F.Cu at (100.2, 77.6)
- added ?: , SMD:0201, F.Cu at (56.6, 36.8)
- added ?: , SMD:0402, F.Cu at (117.5, 94.1)
- added ?: , SMD:0201, F.Cu at (42.9, 82.9)
- added ?: , SMD:0201, F.Cu at (97.4, 44.7)
- added ?: , SMD:0402, F.Cu at (152.5, 55.5)
- added ?: , SMD:0402, F.Cu at (132.7, 80.4)
- added ?: , SMD:0201, F.Cu at (132.8, 95.5)
- added ?: , SMD:0402, F.Cu at (133.7, 92.6)
- added ?: , SMD:0201, F.Cu at (207.3, 40.5)
- added ?: , SMD:0201, F.Cu at (238.7, 123.1)
- added ?: , SMD:0402, F.Cu at (269.2, 10.9)
- added ?: , SMD:0201, F.Cu at (81.3, 135.2)
- added ?: , SMD:0402, F.Cu at (167.2, 21.6)
- added ?: , SMD:0201, F.Cu at (116.2, 129.7)
- added ?: , SMD:0201, F.Cu at (93.4, 14.8)
- added ?: , SMD:0201, F.Cu at (196.4, 38.9)
- added ?: , SMD:0402, F.Cu at (144.1, 97.4)
- added ?: , SMD:0201, F.Cu at (213.8, 47.1)
- added ?: , SMD:0402, F.Cu at (144.8, 88.9)
- added ?: , SMD:0201, F.Cu at (12.9, 62.6)
- added ?: , SMD:0201, F.Cu at (92.3, 29.6)
- added ?: , SMD:0201, F.Cu at (181.2, 63.4)
- added ?: , SMD:0402, F.Cu at (180.0, 18.3)
- added ?: , SMD:0402, F.Cu at (112.3, 62.9)
- added ?: , SMD:0402, F.Cu at (182.1, 118.5)
- added ?: , SMD:0402, F.Cu at (132.9, 120.1)
- added ?: , SMD:0201, F.Cu at (214.7, 8.21)
- added ?: , SMD:0402, F.Cu at (130.7, 99.7)
- added ?: , SMD:0201, F.Cu at (137.6, 81.4)
- added ?: , SMD:0402, F.Cu at (171.5, 100.7)
- added ?: , SMD:0201, F.Cu at (194.4, 118.3)
- added ?: , SMD:0201, F.Cu at (50.9, 55.1)
- added ?: , SMD:0201, F.Cu at (287.8, 48.9)
- added ?: , SMD:0402, F.Cu at (157.4, 37.5)
- added ?: , SMD:0201, F.Cu at (105.2, 53.1)
- added ?: , SMD:0201, F.Cu at (184.8, 37.1)
- added ?: , SMD:0402, F.Cu at (43.8, 133.7)
- added ?: , SMD:0402, F.Cu at (209.3, 43.8)
- added ?: , SMD:0201, F.Cu at (236.3, 138.5)
- added ?: , SMD:0201, F.Cu at (112.6, 53.2)
- added ?: , SMD:0201, F.Cu at (185.7, 75.9)
- added ?: , SMD:0402, F.Cu at (163.1, 51.0)
- added ?: , SMD:0402, F.Cu at (127.3, 89.4)
- added ?: , SMD:0402, F.Cu at (154.0, 96.8)
- added ?: , SMD:0402, F.Cu at (120.9, 12.3)
- added ?: , SMD:0201, F.Cu at (273.6, 30.0)
- added ?: , SMD:0402, F.Cu at (248.2, 113.3)
- added ?: , SMD:0201, F.Cu at (37.9, 124.9)
- added ?: , SMD:0201, F.Cu at (69.6, 133.1)
- added ?: , SMD:0201, F.Cu at (180.7, 11.6)
- added ?: , SMD:0201, F.Cu at (90.5, 115.8)
- added ?: , SMD:0201, F.Cu at (99.1, 15.4)
- added ?: , SMD:0402, F.Cu at (114.5, 96.5)
- added ?: , SMD:0201, F.Cu at (90.5, 101.5)
- added ?: , SMD:0201, F.Cu at (108.9, 16.3)
- added ?: , SMD:0201, F.Cu at (80.7, 5.55)
- added ?: , SMD:0201, F.Cu at (124.8, 55.0)
- added ?: , SMD:0201, F.Cu at (92.0, 88.5)
- added ?: , SMD:0402, F.Cu at (119.0, 79.1)
- added ?: , SMD:0201, F.Cu at (232.1, 15.8)
- added ?: , SMD:0402, F.Cu at (145.3, 53.3)
- added ?: , SMD:0201, F.Cu at (93.5, 120.4)
- added ?: , SMD:0201, F.Cu at (226.3, 91.6)
- added ?: , SMD:0201, F.Cu at (106.2, 1.45)
- added ?: , SMD:0402, F.Cu at (61.5, 119.0)
- added ?: , SMD:0201, F.Cu at (168.6, 109.9)
- added ?: , SMD:0201, F.Cu at (181.5, 74.9)
- added ?: , SMD:0201, F.Cu at (150.5, 64.5)
- added ?: , SMD:0201, F.Cu at (77.8, 70.6)
- added ?: , SMD:0402, F.Cu at (118.5, 50.3)
- added ?: , SMD:0201, F.Cu at (203.0, 98.9)
- added ?: , SMD:0201, F.Cu at (163.1, 100.3)
- added ?: , SMD:0402, F.Cu at (156.0, 62.1)
- added ?: , SMD:0402, F.Cu at (273.2, 109.2)
- added ?: , SMD:0201, F.Cu at (144.3, 96.2)
- added ?: , SMD:0402, F.Cu at (151.1, 60.2)
- added ?: , SMD:0201, F.Cu at (136.5, 72.5)
- added ?: , SMD:0201, F.Cu at (200.2, 26.4)
- added ?: , SMD:0201, F.Cu at (107.6, 95.5)
- added ?: , SMD:0201, F.Cu at (217.8, 125.6)
- added ?: , SMD:0402, F.Cu at (68.7, 7.14)
- added ?: , SMD:0402, F.Cu at (225.9, 67.6)
- added ?: , SMD:0402, F.Cu at (62.1, 72.0)
- added ?: , SMD:0201, F.Cu at (140.8, 105.2)
- added ?: , SMD:0201, F.Cu at (129.6, 74.6)
- added ?: , SMD:0402, F.Cu at (262.9, 69.3)
- added ?: , SMD:0201, F.Cu at (103.5, 51.5)
- added ?: , SMD:0402, F.Cu at (185.8, 86.3)
- added ?: , SMD:0201, F.Cu at (243.5, 73.3)
- added ?: , SMD:0201, F.Cu at (110.3, 100.4)
- added ?: , SMD:0402, F.Cu at (165.7, 43.0)
- added ?: , SMD:0402, F.Cu at (101.2, 19.8)
- added ?: , SMD:0201, F.Cu at (55.0, 127.0)
- added ?: , SMD:0402, F.Cu at (229.4, 79.4)
- added ?: , SMD:0201, F.Cu at (158.2, 81.2)
- added ?: , SMD:0402, F.Cu at (42.9, 18.8)
- added ?: , SMD:0402, F.Cu at (206.3, 5.83)
- added ?: , SMD:0402, F.Cu at (162.0, 58.3)
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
